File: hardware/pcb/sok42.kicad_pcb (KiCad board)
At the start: 2 copper layers, 133 x 122 mm, 197 parts, among them J0 USB_C_Receptacle_USB2.0, J1 USB_C_Receptacle_USB2.0, J2 Conn_01x06, J3 Conn_01x06, J4 Conn_01x04, Q0 BSS138, Q1 BSS138, Q2 BSS138, Q3 BSS138, Q4 BSS138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

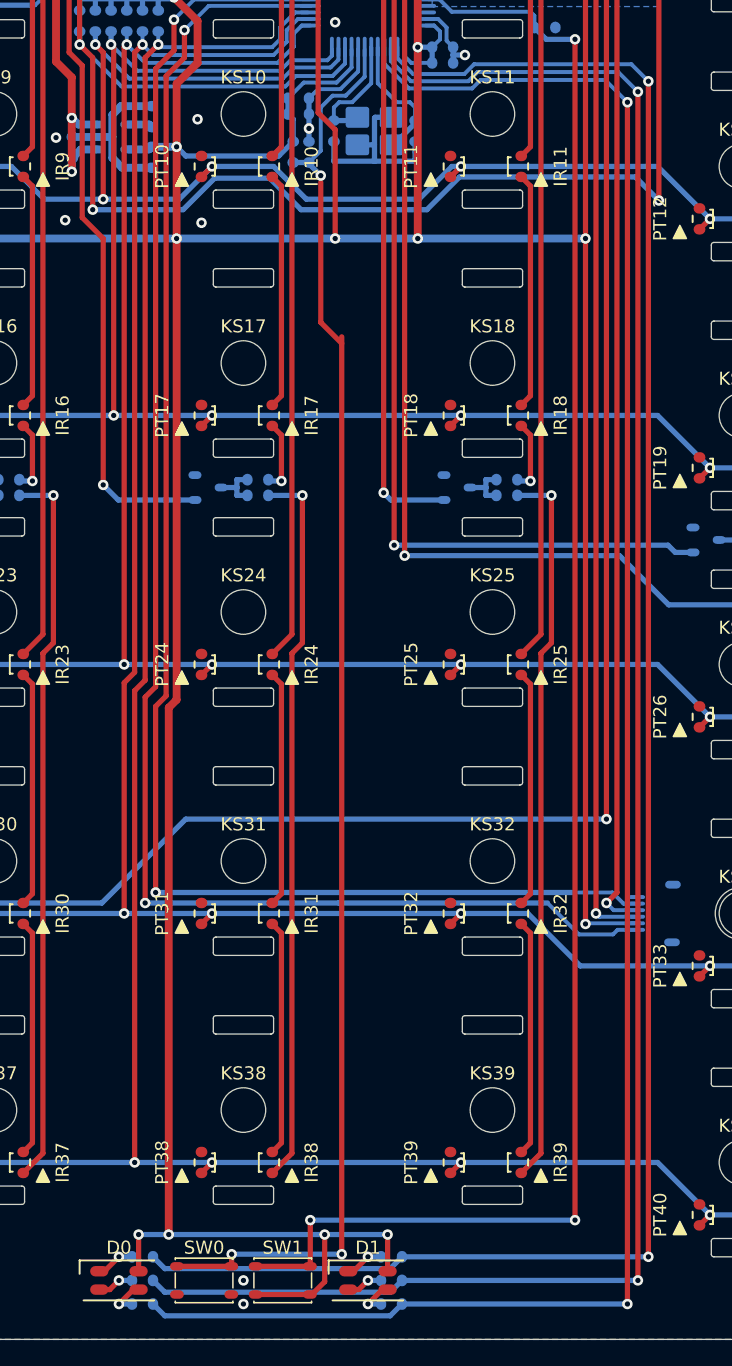
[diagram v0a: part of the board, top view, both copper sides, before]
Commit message: hw/pcb: remove led
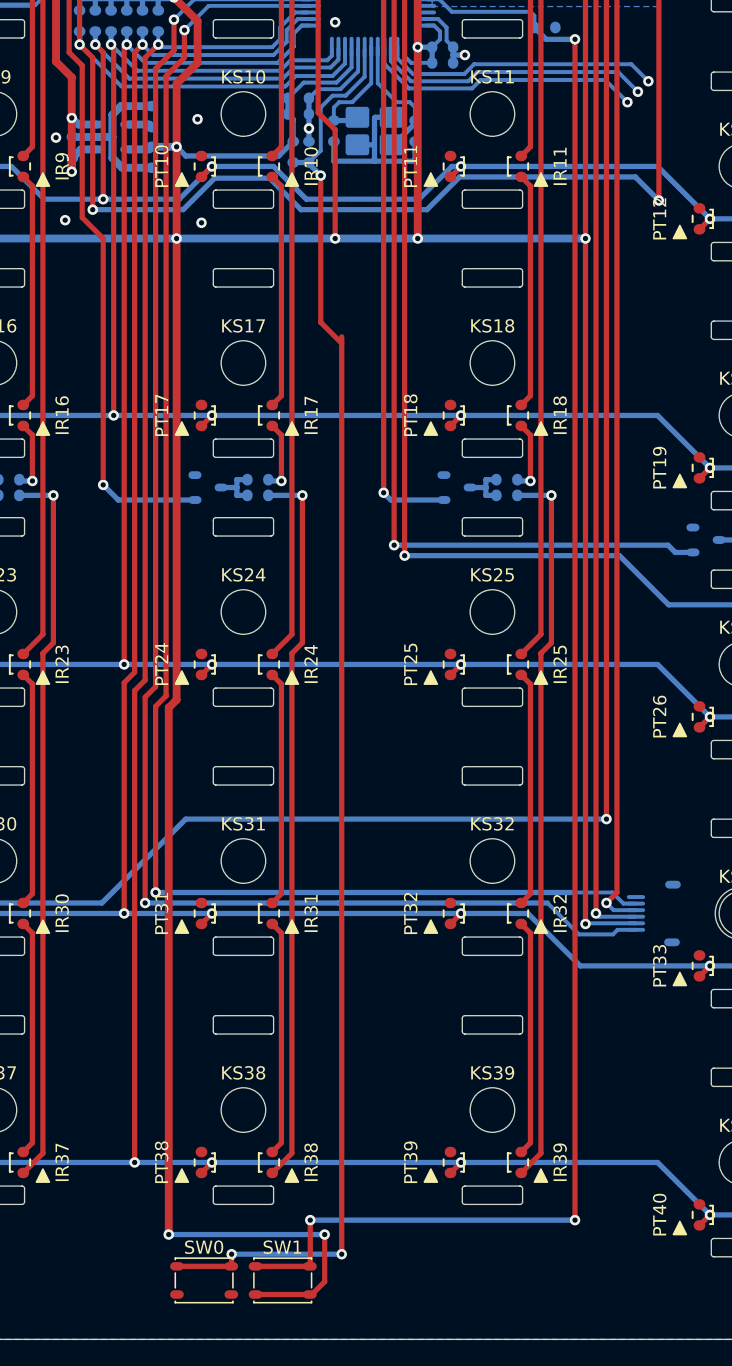
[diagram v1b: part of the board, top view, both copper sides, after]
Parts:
- removed D0, D1: LED_RABG, sok42:LED_RGB_PLCC4
- removed R10, R11, R12, R7, R8, R9: 1k, sok42:RC_0603_1608Metric
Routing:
- net led_b: track 150.2 -> 21.6 mm, vias 2 -> 1
- net led_g: track 149.9 -> 21.5 mm, vias 2 -> 1
- net led_r: track 149.6 -> 21.4 mm, vias 2 -> 1
- net +3.3V: track 440.7 -> 428.0 mm, vias 18 -> 16
- net Net-(D1-Pad3): track 2.96 -> 0.00 mm, vias 1 -> 0
- net Net-(D1-Pad1): track 2.96 -> 0.00 mm, vias 1 -> 0
- net Net-(D0-Pad3): track 2.96 -> 0.00 mm, vias 1 -> 0
- net Net-(D0-Pad1): track 2.96 -> 0.00 mm, vias 1 -> 0
- net Net-(D1-Pad4): track 2.79 -> 0.00 mm, vias 1 -> 0
- net Net-(D0-Pad4): track 2.79 -> 0.00 mm, vias 1 -> 0
- net GND: vias 22 -> 20
